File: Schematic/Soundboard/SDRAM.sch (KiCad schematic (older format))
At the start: 2 parts, among them U1 STM32f429IIT6-units, U8 IS42S16400J-xC

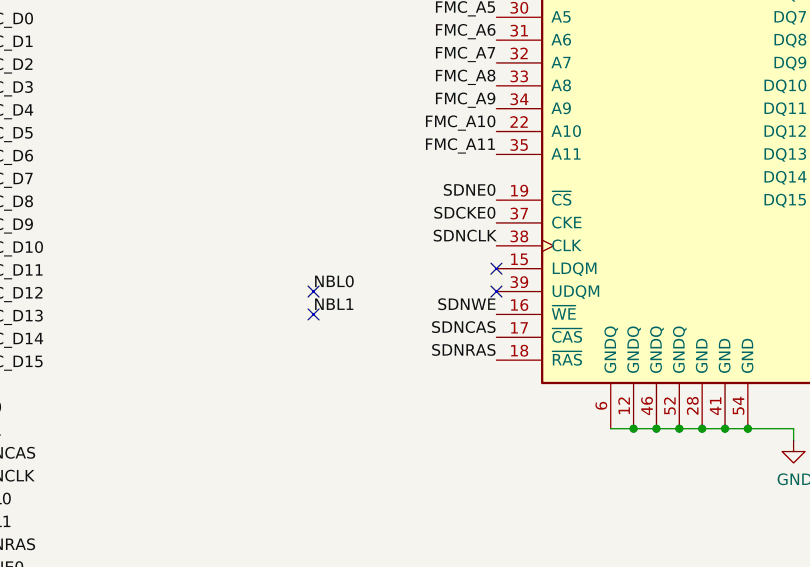
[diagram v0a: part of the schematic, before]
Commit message: Complete connections except for display to be chosen
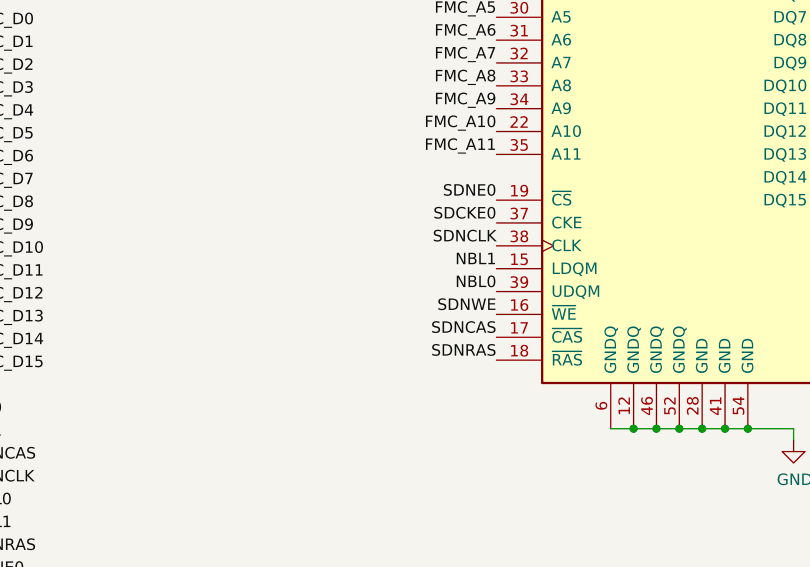
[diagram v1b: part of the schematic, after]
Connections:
- net NBL0: now also U8.39 (UDQM)
- net NBL1: now also U8.15 (LDQM)
- no-connect marks 5 -> 1
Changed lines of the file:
@@
 Text Label 5100 4150 2    50   ~ 0
 SDNCLK
-Text Label 4300 4350 0    50   ~ 0
+Text Label 5100 4350 2    50   ~ 0
 NBL0
-Text Label 4300 4450 0    50   ~ 0
+Text Label 5100 4250 2    50   ~ 0
 NBL1
 Text Label 5100 4650 2    50   ~ 0
@@
 	1    0    0    -1
 $EndComp
-NoConn ~ 4300 4450
-NoConn ~ 4300 4350
-NoConn ~ 5100 4350
-NoConn ~ 5100 4250
 $EndSCHEMATC

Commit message: Additional rework
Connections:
- net BA0: now also U1.108 (PG4)
- net BA1: now also U1.109 (PG5)
- net FMC_A0: now also U1.16 (PF0)
- net FMC_A1: now also U1.17 (PF1)
- net FMC_A10: now also U1.66 (PG0)
- net FMC_A11: now also U1.67 (PG1)
- net FMC_A2: now also U1.18 (PF2)
- net FMC_A3: now also U1.19 (PF3)
- net FMC_A4: now also U1.20 (PF4)
- net FMC_A5: now also U1.21 (PF5)
- net FMC_A6: now also U1.60 (PF12)
- net FMC_A7: now also U1.63 (PF13)
- net FMC_A8: now also U1.64 (PF14)
- net FMC_A9: now also U1.65 (PF15)
- net FMC_D0: now also U1.104 (PD14)
- net FMC_D1: now also U1.105 (PD15)
- net FMC_D10: now also U1.76 (PE13)
- net FMC_D11: now also U1.77 (PE14)
- net FMC_D12: now also U1.78 (PE15)
- net FMC_D13: now also U1.96 (PD8)
- net FMC_D14: now also U1.97 (PD9)
- net FMC_D15: now also U1.98 (PD10)
- net FMC_D2: now also U1.142 (PD0)
- net FMC_D3: now also U1.143 (PD1)
- net FMC_D4: now also U1.68 (PE7)
- net FMC_D5: now also U1.69 (PE8)
- net FMC_D6: now also U1.70 (PE9)
- net FMC_D7: now also U1.73 (PE10)
- net FMC_D8: now also U1.74 (PE11)
- net FMC_D9: now also U1.75 (PE12)
- net NBL0: now also U1.169 (PE0)
- net NBL1: now also U1.170 (PE1)
- net SDCKE0: now also U1.35 (PC3)
- net SDNCAS: now also U1.160 (PG15)
- net SDNCLK: now also U1.112 (PG8)
- net SDNE0: now also U1.34 (PC2)
- net SDNRAS: now also U1.59 (PF11)
- net SDNWE: now also U1.32 (PC0)
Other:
- moved on the sheet: U1D
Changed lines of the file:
@@
 EESchema Schematic File Version 4
-LIBS:Soundboard-cache
-EELAYER 26 0
+EELAYER 30 0
 EELAYER END
 $Descr A4 11693 8268
@@
 L Soundboard:STM32f429IIT6-units U1
 U 4 1 5F59D5B5
-P 2000 1550
-F 0 "U1" H 2256 1565 50  0000 C CNN
-F 1 "STM32f429IIT6-units" H 2256 1474 50  0000 C CNN
-F 2 "" H 2000 1550 50  0001 C CNN
-F 3 "" H 2000 1550 50  0001 C CNN
-	4    2000 1550
+P 2150 1600
+F 0 "U1" H 2406 1615 50  0000 C CNN
+F 1 "STM32f429IIT6-units" H 2406 1524 50  0000 C CNN
+F 2 "" H 2150 1600 50  0001 C CNN
+F 3 "" H 2150 1600 50  0001 C CNN
+	4    2150 1600
 	1    0    0    -1
 $EndComp

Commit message: Choose display. Complete schematic
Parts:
- U1: footprint (none) -> Package_QFP:LQFP-176_24x24mm_P0.5mm
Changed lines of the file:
@@
 F 0 "U1" H 2406 1615 50  0000 C CNN
 F 1 "STM32f429IIT6-units" H 2406 1524 50  0000 C CNN
-F 2 "" H 2150 1600 50  0001 C CNN
+F 2 "Package_QFP:LQFP-176_24x24mm_P0.5mm" H 2150 1600 50  0001 C CNN
 F 3 "" H 2150 1600 50  0001 C CNN
 	4    2150 1600
